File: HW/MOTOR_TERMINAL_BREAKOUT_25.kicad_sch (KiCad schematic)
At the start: 17 parts

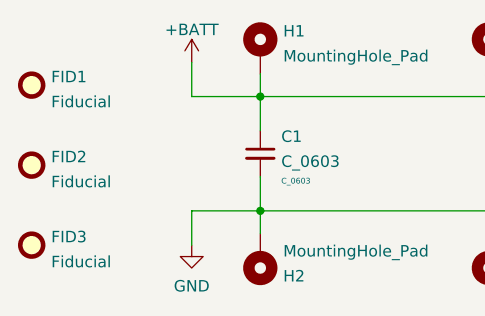
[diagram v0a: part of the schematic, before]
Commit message: Make Minor Updates to Mount Holes and Silkscreen
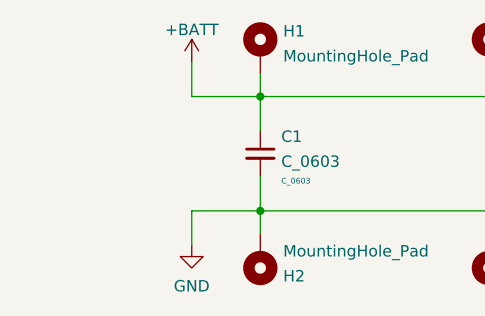
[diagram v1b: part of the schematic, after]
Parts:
- removed FID1, FID2, FID3: Fiducial, Fiducial:Fiducial_0.5mm_Mask1mm, symbol Mechanical:Fiducial
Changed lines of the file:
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@@
     (pin "1")
-  )
-  (symbol (lib_id "Mechanical:Fiducial") (at 134.62 156.21 0) (unit 1)
-    (in_bom yes) (on_board yes) (fields_autoplaced)
-    (property "Reference" "FID3" (id 0) (at 136.779 155.3015 0)
-      (effects (font (size 1.27 1.27)) (justify left))
-    )
-    (property "Value" "Fiducial" (id 1) (at 136.779 158.0766 0)
-      (effects (font (size 1.27 1.27)) (justify left))
-    )
-    (property "Footprint" "Fiducial:Fiducial_0.5mm_Mask1mm" (id 2) (at 134.62 156.21 0)
-      (effects (font (size 1.27 1.27)) hide)
-    )
-    (property "Datasheet" "~" (id 3) (at 134.62 156.21 0)
-      (effects (font (size 1.27 1.27)) hide)
-    )
   )
   (symbol (lib_id "Mechanical:MountingHole_Pad") (at 234.95 157.48 0) (mirror x) (unit 1)
@@
     )
     (pin "1")
-  )
-  (symbol (lib_id "Mechanical:Fiducial") (at 134.62 138.43 0) (unit 1)
-    (in_bom yes) (on_board yes) (fields_autoplaced)
-    (property "Reference" "FID1" (id 0) (at 136.779 137.5215 0)
-      (effects (font (size 1.27 1.27)) (justify left))
-    )
-    (property "Value" "Fiducial" (id 1) (at 136.779 140.2966 0)
-      (effects (font (size 1.27 1.27)) (justify left))
-    )
-    (property "Footprint" "Fiducial:Fiducial_0.5mm_Mask1mm" (id 2) (at 134.62 138.43 0)
-      (effects (font (size 1.27 1.27)) hide)
-    )
-    (property "Datasheet" "~" (id 3) (at 134.62 138.43 0)
-      (effects (font (size 1.27 1.27)) hide)
-    )
   )
   (symbol (lib_id "C_Capacitor:C_0603") (at 160.02 146.05 0) (unit 1)
@@
     )
     (pin "1")
-  )
-  (symbol (lib_id "Mechanical:Fiducial") (at 134.62 147.32 0) (unit 1)
-    (in_bom yes) (on_board yes) (fields_autoplaced)
-    (property "Reference" "FID2" (id 0) (at 136.779 146.4115 0)
-      (effects (font (size 1.27 1.27)) (justify left))
-    )
-    (property "Value" "Fiducial" (id 1) (at 136.779 149.1866 0)
-      (effects (font (size 1.27 1.27)) (justify left))
-    )
-    (property "Footprint" "Fiducial:Fiducial_0.5mm_Mask1mm" (id 2) (at 134.62 147.32 0)
-      (effects (font (size 1.27 1.27)) hide)
-    )
-    (property "Datasheet" "~" (id 3) (at 134.62 147.32 0)
-      (effects (font (size 1.27 1.27)) hide)
-    )
   )
   (symbol (lib_id "Mechanical:MountingHole_Pad") (at 209.55 134.62 0) (unit 1)
@@
       (reference "C1") (unit 1) (value "C_0603") (footprint "C_Capacitor:C_0603")
     )
-    (path "/6e4bbe2c-1e2d-4539-b6d8-5d5edc57b4de"
-      (reference "FID1") (unit 1) (value "Fiducial") (footprint "Fiducial:Fiducial_0.5mm_Mask1mm")
-    )
-    (path "/e42b8b80-020c-4fee-b000-fd91abf3966d"
-      (reference "FID2") (unit 1) (value "Fiducial") (footprint "Fiducial:Fiducial_0.5mm_Mask1mm")
-    )
-    (path "/1cb64bfe-d819-47e3-be11-515b04f2c451"
-      (reference "FID3") (unit 1) (value "Fiducial") (footprint "Fiducial:Fiducial_0.5mm_Mask1mm")
-    )
     (path "/b5969789-f675-41e8-a4df-8b0b8a8e4ee2"

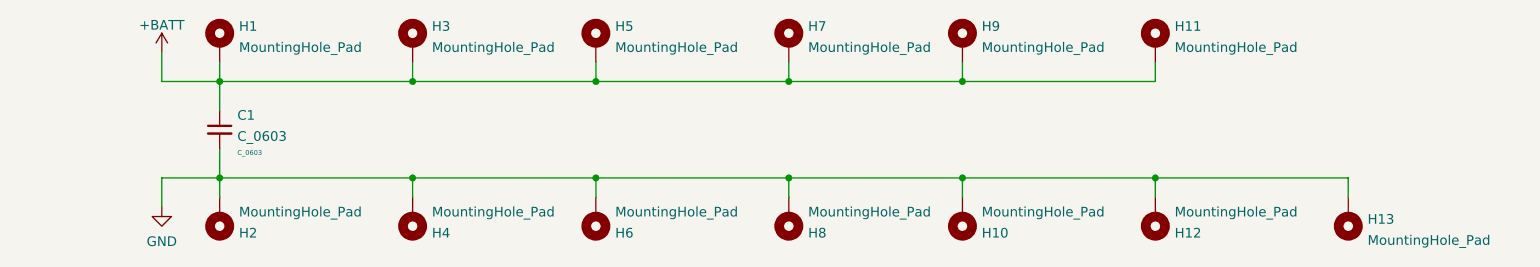
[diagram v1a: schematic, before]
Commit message: Adjust Hole Positions to Account For Terminal Angle on Motor
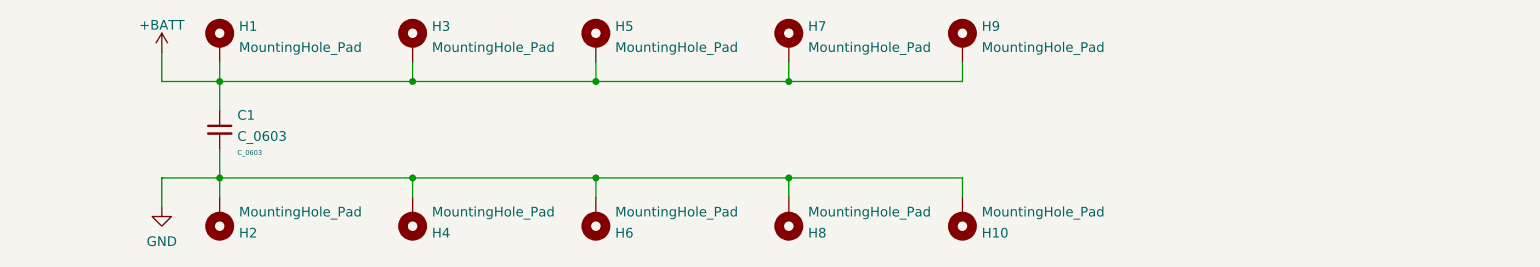
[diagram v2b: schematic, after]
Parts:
- removed H11, H12: MountingHole_Pad, MountingHole:MountingHole_3.2mm_M3_ISO7380_Pad_TopBottom, symbol Mechanical:MountingHole_Pad
- removed H13: MountingHole_Pad, MountingHole:MountingHole_6.5mm, symbol Mechanical:MountingHole_Pad
- H10, H3, H4, H5, H6, H7, H8, H9: footprint MountingHole:MountingHole_3.2mm_M3_ISO7380_Pad_TopBottom -> MountingHole:MountingHole_3mm_Pad_TopBottom

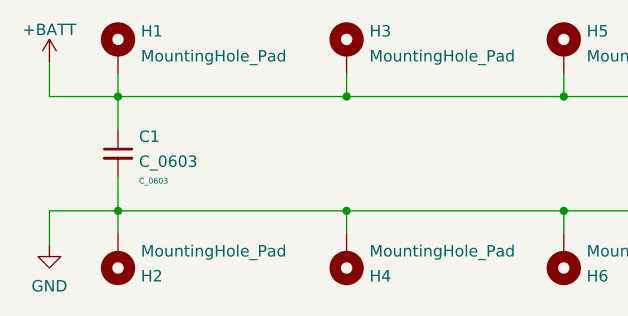
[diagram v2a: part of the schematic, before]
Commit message: Fix issue hole position issue.
Holes positions did not allow motor terminals to align with bolt holes
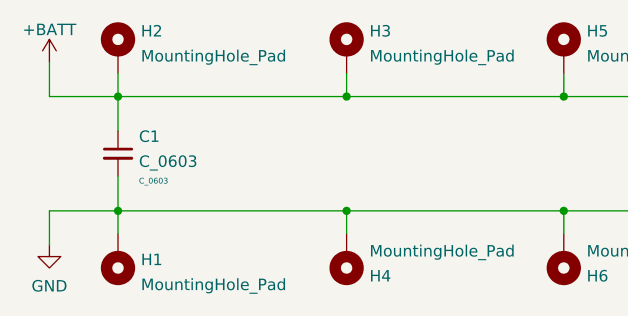
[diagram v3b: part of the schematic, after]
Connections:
- net +BATT: now also H2.1; no longer H1.1
- net GND: now also H1.1; no longer H2.1
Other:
- moved on the sheet: H1, H2
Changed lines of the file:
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@@
-    (stroke (width 0) (type default) (color 0 0 0 0))
-  )
-  (wire (pts (xy 160.02 152.4) (xy 160.02 154.94))
     (stroke (width 0) (type default) (color 0 0 0 0))
   )
@@
     (stroke (width 0) (type default) (color 0 0 0 0))
   )
+  (wire (pts (xy 160.02 154.94) (xy 160.02 152.4))
+    (stroke (width 0) (type default) (color 0 0 0 0))
+  )
   (wire (pts (xy 152.4 139.7) (xy 160.02 139.7))
     (stroke (width 0) (type default) (color 0 0 0 0))
@@
     (stroke (width 0) (type default) (color 0 0 0 0))
   )
+  (wire (pts (xy 160.02 139.7) (xy 160.02 137.16))
+    (stroke (width 0) (type default) (color 0 0 0 0))
+  )
   (wire (pts (xy 234.95 137.16) (xy 234.95 139.7))
     (stroke (width 0) (type default) (color 0 0 0 0))
   )
   (wire (pts (xy 185.42 152.4) (xy 209.55 152.4))
-    (stroke (width 0) (type default) (color 0 0 0 0))
-  )
-  (wire (pts (xy 160.02 137.16) (xy 160.02 139.7))
     (stroke (width 0) (type default) (color 0 0 0 0))
   )
@@
     (pin "1")
   )
-  (symbol (lib_id "Mechanical:MountingHole_Pad") (at 160.02 134.62 0) (unit 1)
+  (symbol (lib_id "Mechanical:MountingHole_Pad") (at 160.02 157.48 180) (unit 1)
     (in_bom yes) (on_board yes) (fields_autoplaced)
-    (property "Reference" "H1" (id 0) (at 162.56 132.4415 0)
-      (effects (font (size 1.27 1.27)) (justify left))
-    )
-    (property "Value" "MountingHole_Pad" (id 1) (at 162.56 135.2166 0)
-      (effects (font (size 1.27 1.27)) (justify left))
-    )
-    (property "Footprint" "MountingHole:MountingHole_3.2mm_M3_ISO7380_Pad_TopBottom" (id 2) (at 160.02 134.62 0)
-      (effects (font (size 1.27 1.27)) hide)
-    )
-    (property "Datasheet" "~" (id 3) (at 160.02 134.62 0)
+    (property "Reference" "H1" (id 0) (at 162.56 157.8415 0)
+      (effects (font (size 1.27 1.27)) (justify right))
+    )
+    (property "Value" "MountingHole_Pad" (id 1) (at 162.56 160.6166 0)
+      (effects (font (size 1.27 1.27)) (justify right))
+    )
+    (property "Footprint" "MountingHole:MountingHole_3.2mm_M3_ISO7380_Pad_TopBottom" (id 2) (at 160.02 157.48 0)
+      (effects (font (size 1.27 1.27)) hide)
+    )
+    (property "Datasheet" "~" (id 3) (at 160.02 157.48 0)
       (effects (font (size 1.27 1.27)) hide)
     )
@@
     (pin "1")
   )
-  (symbol (lib_id "Mechanical:MountingHole_Pad") (at 160.02 157.48 0) (mirror x) (unit 1)
+  (symbol (lib_id "Mechanical:MountingHole_Pad") (at 160.02 134.62 0) (mirror y) (unit 1)
     (in_bom yes) (on_board yes) (fields_autoplaced)
-    (property "Reference" "H2" (id 0) (at 162.56 159.6585 0)
-      (effects (font (size 1.27 1.27)) (justify left))
-    )
-    (property "Value" "MountingHole_Pad" (id 1) (at 162.56 156.8834 0)
-      (effects (font (size 1.27 1.27)) (justify left))
-    )
-    (property "Footprint" "MountingHole:MountingHole_3.2mm_M3_ISO7380_Pad_TopBottom" (id 2) (at 160.02 157.48 0)
-      (effects (font (size 1.27 1.27)) hide)
-    )
-    (property "Datasheet" "~" (id 3) (at 160.02 157.48 0)
-      (effects (font (size 1.27 1.27)) hide)
-    )
+    (property "Reference" "H2" (id 0) (at 162.56 132.4415 0)
+      (effects (font (size 1.27 1.27)) (justify right))
+    )
+    (property "Value" "MountingHole_Pad" (id 1) (at 162.56 135.2166 0)
+      (effects (font (size 1.27 1.27)) (justify right))
+    )
+    (property "Footprint" "MountingHole:MountingHole_3.2mm_M3_ISO7380_Pad_TopBottom" (id 2) (at 160.02 134.62 0)
+      (effects (font (size 1.27 1.27)) hide)
+    )
+    (property "Datasheet" "~" (id 3) (at 160.02 134.62 0)
+      (effects (font (size 1.27 1.27)) hide)
+    )
